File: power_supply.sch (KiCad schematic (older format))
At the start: 0 parts

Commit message: Scheme for 5V Main DC/DC converter created
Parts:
- added BAT?: BU1632SM, antmicro-footprints:BU1632SM, symbol antmicroBatteryHoldersClipsContacts:BU1632SM
- added C? (x3): C_2u2_0805_50V, antmicro-footprints:0805-cap, symbol antmicroCapacitorsmisc:C_2u2_0805_50V
- added C?: C_10n_0402, antmicro-footprints:0402-cap, symbol antmicroCapacitors0402:C_10n_0402
- added C?: C_4n7_0805, antmicro-footprints:0402-cap, symbol antmicroCapacitors0402:C_4n7_0402
- added C?: C_47p_0402, antmicro-footprints:0402-cap, symbol antmicroCapacitors0402:C_47p_0402
- added C?: C_100n_0402, antmicro-footprints:0402-cap, symbol antmicroCapacitors0402:C_100n_0402
- added C? (x3): C_47u_0603, antmicro-footprints:0603-cap, symbol antmicroCapacitors0603:C_47u_0603
- added D??: PDS760-13, antmicro-footprints:PDS760-13, symbol antmicroDiodesRectifiersSingle:PDS760-13
- added IC?: TPS54561DPRT, antmicro-footprints:WSON-10_4x4, symbol antmicroPMICVoltageRegulatorsLinear:TPS54561DPRT
- added J?: PJ-202A, antmicro-footprints:Barrel_Jack_5.5mmODx2.1mmID_PJ-202A, symbol antmicroBarrelPowerConnectors:PJ-202A
- added L?: 7447798720, antmicro-footprints:WE_7447798720, symbol antmicroFixedInductors:7447798720
- added R?: R_243k_0402, antmicro-footprints:0402-res, symbol antmicroResistors0402:R_243k_0402
- added R?: R_16k9_0402, antmicro-footprints:0402-res, symbol antmicroResistors0402:R_16k9_0402
- added R?: R_100k_0402, antmicro-footprints:0402-res, symbol antmicroResistors0402:R_100k_0402
- added R?: R_49R9_0603, antmicro-footprints:0603-res, symbol antmicroResistors0603:R_49R9_0603
- added R?: R_53k6_0402, antmicro-footprints:0402-res, symbol antmicroResistors0402:R_53k6_0402
- added R?: R_10k2_0402, antmicro-footprints:0402-res, symbol antmicroResistors0402:R_10k2_0402
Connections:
- net labels added: +5V, GND, RTC_BAT, VCC
- wire segments 0 -> 52
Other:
- note added: "3V3 LDO"
- note added: "4.5V step down from 5V Buck"
- note added: "5V Main DC/DC"
- note added: "Power input"
- note added: "RTC"

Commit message: Added scheme for 5V to 3V3 buck
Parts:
- added C?: C_2u2_0402, antmicro-footprints:0402-cap, symbol antmicroCapacitors0402:C_2u2_0402
- added C?: C_100p_0603, antmicro-footprints:0603-cap, symbol antmicroCapacitors0603:C_100p_0603
- added C?: C_10u_0402, antmicro-footprints:0402-cap, symbol antmicroCapacitors0402:C_10u_0402
- added L?: IHLP1212AEERR47M11, antmicro-footprints:IHLP-1212AE, symbol antmicroFixedInductors:IHLP1212AEERR47M11
- added R?: R_10k_0402, antmicro-footprints:0402-res, symbol antmicroResistors0402:R_10k_0402
- added R?: R_243k_0402, antmicro-footprints:0402-res, symbol antmicroResistors0402:R_243k_0402
- added R?: R_53k6_0402, antmicro-footprints:0402-res, symbol antmicroResistors0402:R_53k6_0402
- added U?: TPS62823DLCT, antmicro-footprints:QFN-8_2x1mm, symbol antmicroDCDCConverters:TPS62823DLCT
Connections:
- net labels added: #RESET, 3V3_SYS, V_SOM
- net labels removed: +5V
- wire segments 52 -> 72
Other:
- note added: "5V to 3V3 DC/DC System\n"
- note removed: "3V3 LDO"

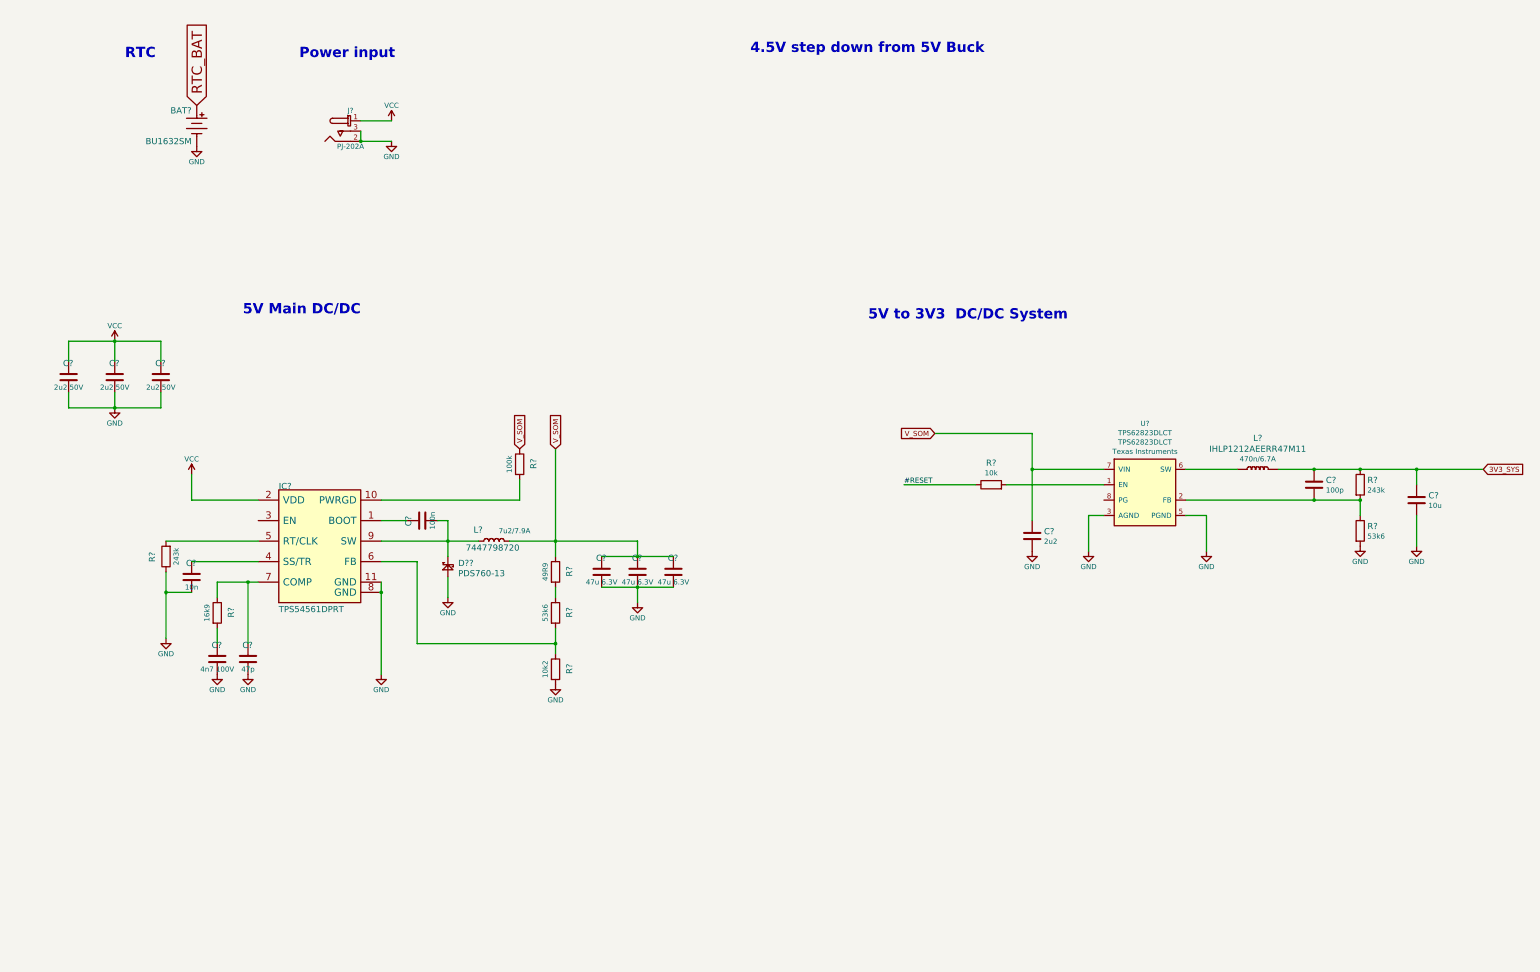
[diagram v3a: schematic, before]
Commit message: Added 5V to 4V SoM power supply and 5V to 3V3 camera power supply
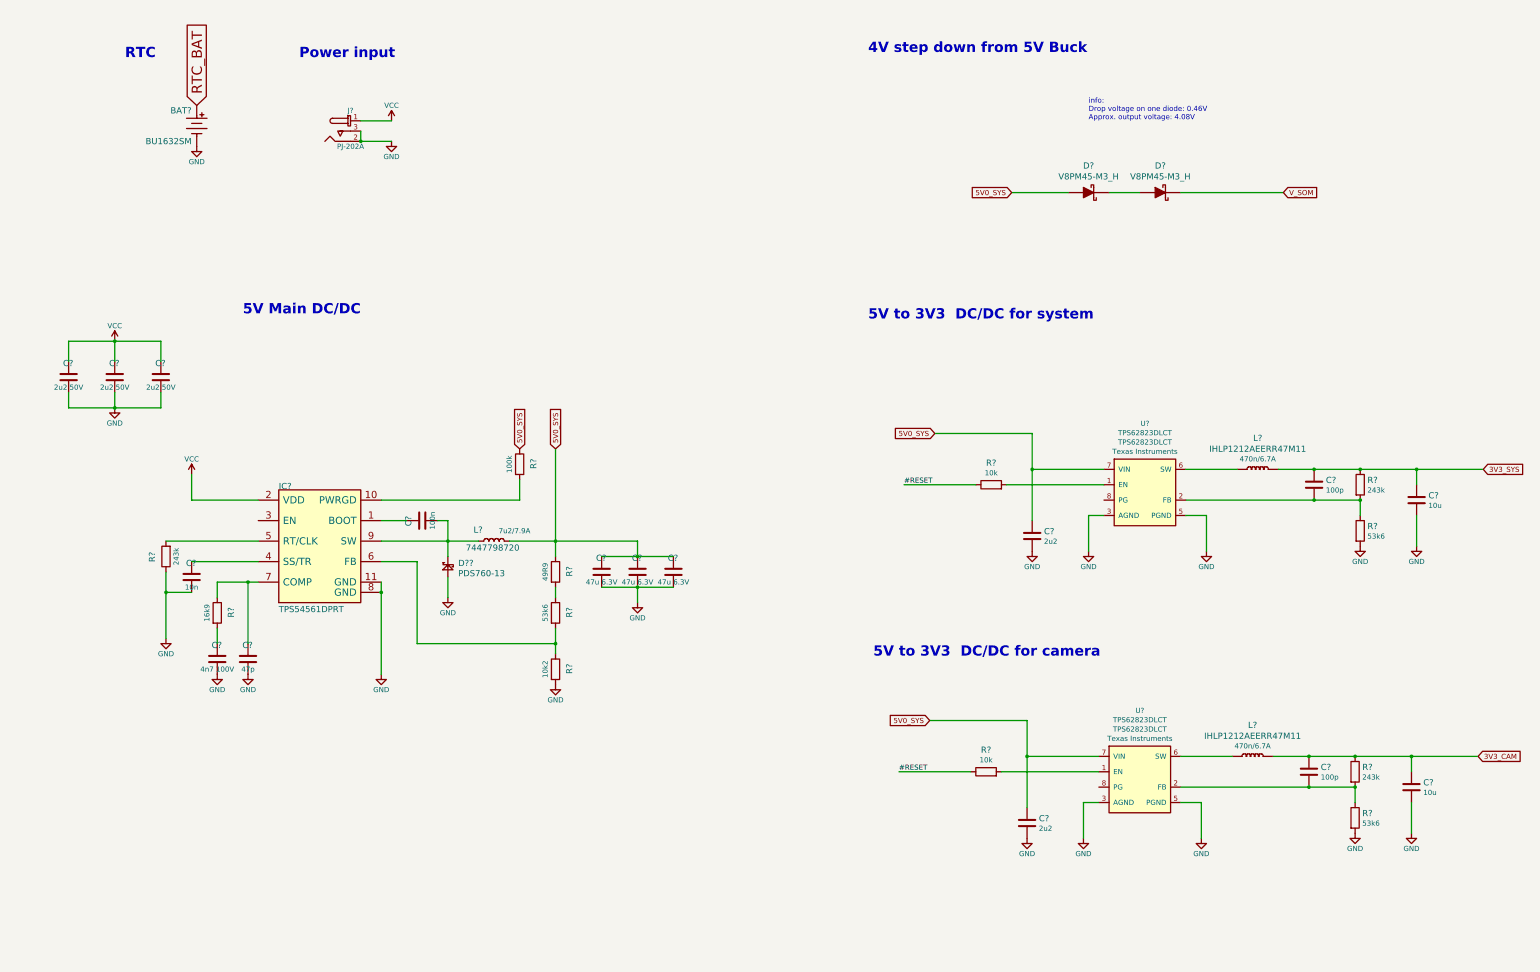
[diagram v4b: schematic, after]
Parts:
- added C?: C_2u2_0402, antmicro-footprints:0402-cap, symbol antmicroCapacitors0402:C_2u2_0402
- added C?: C_100p_0603, antmicro-footprints:0603-cap, symbol antmicroCapacitors0603:C_100p_0603
- added C?: C_10u_0402, antmicro-footprints:0402-cap, symbol antmicroCapacitors0402:C_10u_0402
- added D? (x2): V8PM45-M3_H, face-scanner-led-board-footprints:TO-277A, symbol antmicroDiodesRectifiersSingle:V8PM45-M3_H
- added L?: IHLP1212AEERR47M11, antmicro-footprints:IHLP-1212AE, symbol antmicroFixedInductors:IHLP1212AEERR47M11
- added R?: R_10k_0402, antmicro-footprints:0402-res, symbol antmicroResistors0402:R_10k_0402
- added R?: R_243k_0402, antmicro-footprints:0402-res, symbol antmicroResistors0402:R_243k_0402
- added R?: R_53k6_0402, antmicro-footprints:0402-res, symbol antmicroResistors0402:R_53k6_0402
- added U?: TPS62823DLCT, antmicro-footprints:QFN-8_2x1mm, symbol antmicroDCDCConverters:TPS62823DLCT
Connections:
- net #RESET: now also R?.1
- net GND: now also C?.2, C?.2, R?.2, U?.3 (AGND), U?.5 (PGND)
- net V_SOM: now also D?.3; no longer C?.1, C?.1, C?.1, C?.1, L?.2 (P), R?.1, R?.1, U?.7 (VIN)
- new net: D?.1, D?.2, D?.3
- new net: R?.2, U?.1 (EN)
- new net: C?.2, R?.1, R?.2, U?.2 (FB)
- new net: L?.1 (P), U?.6 (SW)
- new net 3V3_CAM: C?.1, C?.1, L?.2 (P), R?.1
- new net 5V0_SYS: C?.1, C?.1, C?.1, C?.1, C?.1, D?.1, D?.2, L?.2 (P), R?.1, R?.1, U?.7 (VIN), U?.7 (VIN)
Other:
- note added: "4V step down from 5V Buck"
- note added: "5V to 3V3 DC/DC for camera\n\n"
- note added: "5V to 3V3 DC/DC for system\n"
- note added: "info: \nDrop voltage on one diode: 0.46V\nApprox. output voltage: 4.08V"
- note removed: "4.5V step down from 5V Buck"
- note removed: "5V to 3V3 DC/DC System\n"

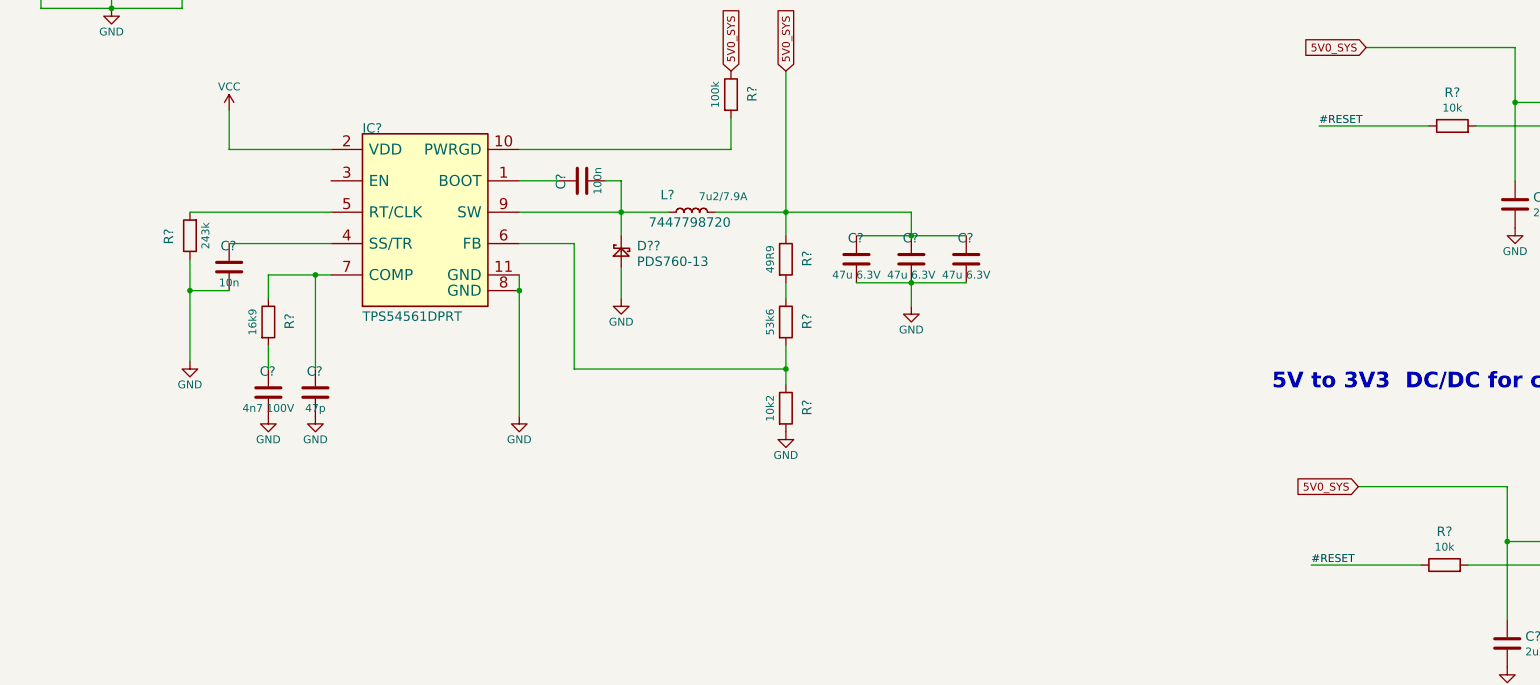
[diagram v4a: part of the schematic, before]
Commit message: Creating schemas for camera FFC, connecting related pins to SoM, schema of I2C MUX and voltage transceiver; Adding RESET to power supplies; connecting to SoM 1v8 power output
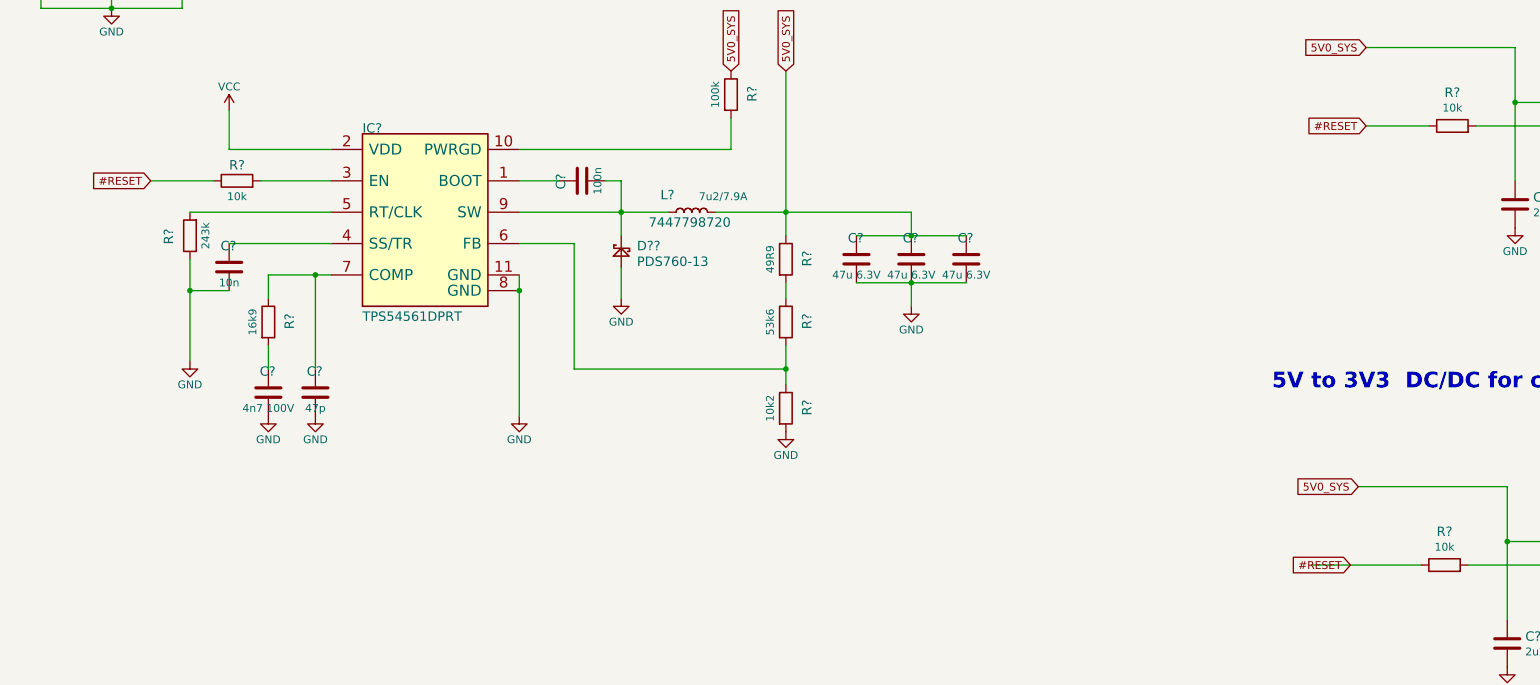
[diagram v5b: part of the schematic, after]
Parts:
- added R?: R_10k_0402, antmicro-footprints:0402-res, symbol antmicroResistors0402:R_10k_0402
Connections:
- net #RESET: now also R?.1
- net at IC?.3 (EN): now also R?.2
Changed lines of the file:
@@
 Wire Wire Line
 	9900 5300 10850 5300
-Text Label 8900 5300 0    50   ~ 0
-#RESET
-Wire Wire Line
-	8900 5300 9600 5300
 $Comp
 L antmicroCapacitors0402:C_2u2_0402 C?
@@
 Wire Wire Line
 	9850 8100 10800 8100
-Text Label 8850 8100 0    50   ~ 0
-#RESET
 Wire Wire Line
 	8850 8100 9550 8100
@@
 	10100 7600 9150 7600
 Connection ~ 10100 7950
+Text GLabel 9200 5300 0    50   Input ~ 0
+#RESET
+Wire Wire Line
+	9200 5300 9600 5300
+Text GLabel 9100 8100 0    50   Input ~ 0
+#RESET
+$Comp
+L antmicroResistors0402:R_10k_0402 R?
+U 1 1 6204E79B
+P 2000 5650
+F 0 "R?" H 2000 5750 60  0000 C CNN
+F 1 "R_10k_0402" H 2000 5500 60  0001 C CNN
+F 2 "antmicro-footprints:0402-res" H 2200 5850 60  0001 L CNN
+F 3 "" H 2000 5650 50  0001 C CNN
+F 4 "VISHAY" H 2200 6050 60  0001 L CNN "Manufacturer"
+F 5 "CRCW040210K0FKEDHP" H 2200 5950 60  0001 L CNN "MPN"
+F 6 "10k" H 2000 5550 50  0000 C CNN "Val"
+	1    2000 5650
+	1    0    0    -1
+$EndComp
+Text GLabel 1450 5650 0    50   Input ~ 0
+#RESET
+Wire Wire Line
+	1450 5650 1850 5650
+Wire Wire Line
+	2600 5650 2150 5650
 $EndSCHEMATC

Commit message: Added annotations. Move to loclib
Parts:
- BAT1: renamed from BAT?; footprint antmicro-footprints:BU1632SM -> sc606-baseboard-footprints:BU1632SM; symbol antmicroBatteryHoldersClipsContacts:BU1632SM -> sc606-baseboard:BU1632SM
- C17, C18, C19: renamed from C?; footprint antmicro-footprints:0805-cap -> sc606-baseboard-footprints:0805-cap; symbol antmicroCapacitorsmisc:C_2u2_0805_50V -> sc606-baseboard:C_2u2_0805_50V
- C20: renamed from C?; footprint antmicro-footprints:0402-cap -> sc606-baseboard-footprints:0402-cap; symbol antmicroCapacitors0402:C_10n_0402 -> sc606-baseboard:C_10n_0402
- C21: renamed from C?; footprint antmicro-footprints:0402-cap -> sc606-baseboard-footprints:0402-cap; symbol antmicroCapacitors0402:C_4n7_0402 -> sc606-baseboard:C_4n7_0402
- C22: renamed from C?; footprint antmicro-footprints:0402-cap -> sc606-baseboard-footprints:0402-cap; symbol antmicroCapacitors0402:C_47p_0402 -> sc606-baseboard:C_47p_0402
- C23: renamed from C?; footprint antmicro-footprints:0402-cap -> sc606-baseboard-footprints:0402-cap; symbol antmicroCapacitors0402:C_100n_0402 -> sc606-baseboard:C_100n_0402
- C24, C25, C26: renamed from C?; footprint antmicro-footprints:0603-cap -> sc606-baseboard-footprints:0603-cap; symbol antmicroCapacitors0603:C_47u_0603 -> sc606-baseboard:C_47u_0603
- C27, C28: renamed from C?; footprint antmicro-footprints:0402-cap -> sc606-baseboard-footprints:0402-cap; symbol antmicroCapacitors0402:C_2u2_0402 -> sc606-baseboard:C_2u2_0402
- C29, C30: renamed from C?; footprint antmicro-footprints:0603-cap -> sc606-baseboard-footprints:0603-cap; symbol antmicroCapacitors0603:C_100p_0603 -> sc606-baseboard:C_100p_0603
- C31, C32: renamed from C?; footprint antmicro-footprints:0402-cap -> sc606-baseboard-footprints:0402-cap; symbol antmicroCapacitors0402:C_10u_0402 -> sc606-baseboard:C_10u_0402
- D3, D4: renamed from D?; footprint face-scanner-led-board-footprints:TO-277A -> sc606-baseboard-footprints:TO-277A; symbol antmicroDiodesRectifiersSingle:V8PM45-M3_H -> sc606-baseboard:V8PM45-M3_H
- D?1: renamed from D??; footprint antmicro-footprints:PDS760-13 -> sc606-baseboard-footprints:PDS760-13; symbol antmicroDiodesRectifiersSingle:PDS760-13 -> sc606-baseboard:PDS760-13
- IC1: renamed from IC?; footprint antmicro-footprints:WSON-10_4x4 -> sc606-baseboard-footprints:WSON-10_4x4; symbol antmicroPMICVoltageRegulatorsLinear:TPS54561DPRT -> sc606-baseboard:TPS54561DPRT
- J2: renamed from J?; footprint antmicro-footprints:Barrel_Jack_5.5mmODx2.1mmID_PJ-202A -> sc606-baseboard-footprints:Barrel_Jack_5.5mmODx2.1mmID_PJ-202A; symbol antmicroBarrelPowerConnectors:PJ-202A -> sc606-baseboard:PJ-202A
- L1: renamed from L?; footprint antmicro-footprints:WE_7447798720 -> sc606-baseboard-footprints:WE_7447798720; symbol antmicroFixedInductors:7447798720 -> sc606-baseboard:7447798720
- L2, L3: renamed from L?; footprint antmicro-footprints:IHLP-1212AE -> sc606-baseboard-footprints:IHLP-1212AE; symbol antmicroFixedInductors:IHLP1212AEERR47M11 -> sc606-baseboard:IHLP1212AEERR47M11
- R10, R11, R4: renamed from R?; footprint antmicro-footprints:0402-res -> sc606-baseboard-footprints:0402-res; symbol antmicroResistors0402:R_10k_0402 -> sc606-baseboard:R_10k_0402
- R12, R14, R3: renamed from R?; footprint antmicro-footprints:0402-res -> sc606-baseboard-footprints:0402-res; symbol antmicroResistors0402:R_243k_0402 -> sc606-baseboard:R_243k_0402
- R13, R15, R8: renamed from R?; footprint antmicro-footprints:0402-res -> sc606-baseboard-footprints:0402-res; symbol antmicroResistors0402:R_53k6_0402 -> sc606-baseboard:R_53k6_0402
- R5: renamed from R?; footprint antmicro-footprints:0402-res -> sc606-baseboard-footprints:0402-res; symbol antmicroResistors0402:R_16k9_0402 -> sc606-baseboard:R_16k9_0402
- R6: renamed from R?; footprint antmicro-footprints:0402-res -> sc606-baseboard-footprints:0402-res; symbol antmicroResistors0402:R_100k_0402 -> sc606-baseboard:R_100k_0402
- R7: renamed from R?; footprint antmicro-footprints:0603-res -> sc606-baseboard-footprints:0603-res; symbol antmicroResistors0603:R_49R9_0603 -> sc606-baseboard:R_49R9_0603
- R9: renamed from R?; footprint antmicro-footprints:0402-res -> sc606-baseboard-footprints:0402-res; symbol antmicroResistors0402:R_10k2_0402 -> sc606-baseboard:R_10k2_0402
- U1, U2: renamed from U?; footprint antmicro-footprints:QFN-8_2x1mm -> sc606-baseboard-footprints:QFN-8_2x1mm; symbol antmicroDCDCConverters:TPS62823DLCT -> sc606-baseboard:TPS62823DLCT
